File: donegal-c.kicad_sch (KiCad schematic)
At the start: 165 parts, among them J1 Molex-0548190519, J2 ISP, SW1 SW_SPST, SW10 SW_SPST, SW11 SW_SPST, SW12 SW_SPST, SW13 SW_SPST, SW14 SW_SPST, SW15 SW_SPST, SW16 SW_SPST, SW17 SW_SPST, SW18 SW_SPST, SW19 SW_SPST, SW2 SW_SPST, SW20 SW_SPST, SW21 SW_SPST, SW22 SW_SPST, SW23 SW_SPST, SW24 SW_SPST, SW25 SW_SPST, SW26 SW_SPST, SW27 SW_SPST, SW28 SW_SPST, SW29 SW_SPST, SW3 SW_SPST, SW30 SW_SPST, SW31 SW_SPST, SW32 SW_SPST, SW33 SW_SPST, SW34 SW_SPST, SW35 SW_SPST, SW36 SW_SPST, SW37 SW_SPST, SW38 SW_SPST, SW39 SW_SPST, SW4 SW_SPST, SW40 SW_SPST, SW41 SW_SPST, SW42 SW_SPST, SW43 SW_SPST, SW44 SW_SPST, SW45 SW_SPST, SW46 SW_SPST, SW47 SW_SPST, SW48 SW_SPST, SW49 SW_SPST, SW5 SW_SPST, SW50 SW_SPST, SW51 SW_SPST, SW52 SW_SPST, SW53 SW_SPST, SW54 SW_SPST, SW55 SW_SPST, SW56 SW_SPST, SW57 SW_SPST, SW58 SW_SPST, SW59 SW_SPST, SW6 SW_SPST, SW60 SW_SPST, SW61 SW_SPST, SW62 SW_SPST, SW63 SW_SPST, SW64 SW_SPST, SW65 SW_SPST, SW66 SW_SPST, SW67 SW_SPST, SW68 RESET, SW69 BOOT, SW7 SW_SPST, SW70 SW_SPST, SW71 SW_SPST, SW8 SW_SPST, SW9 SW_SPST, U1 ATmega328-PU, Y1 16MHZ

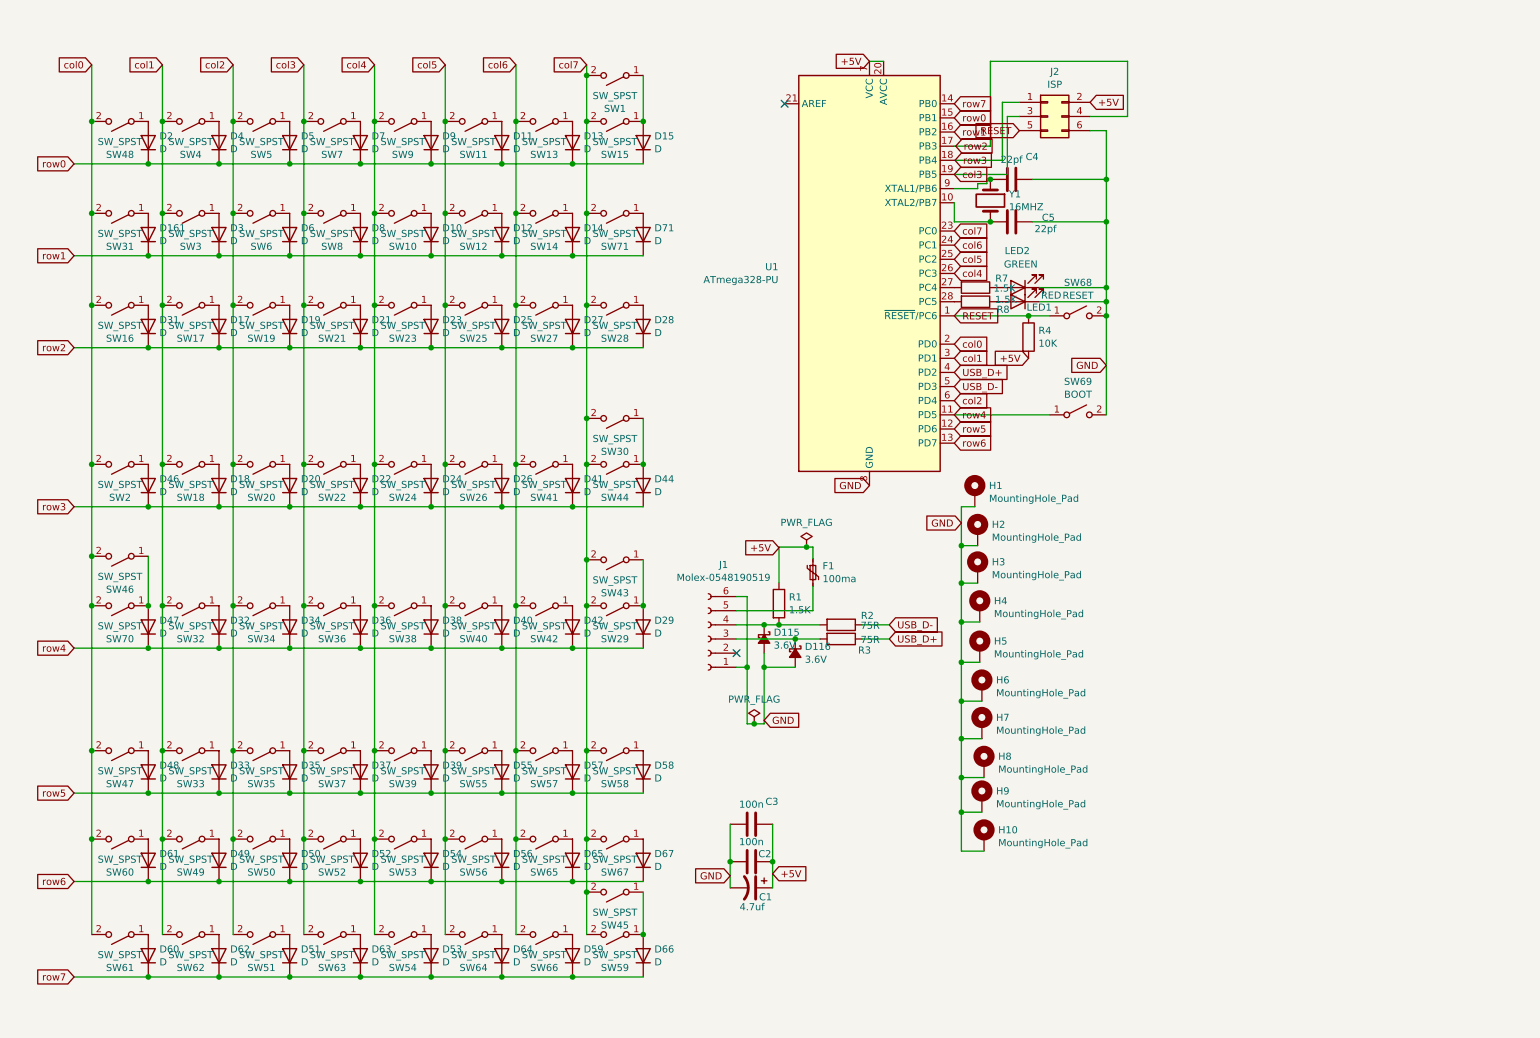
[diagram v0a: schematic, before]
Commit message: Replace Mini USB with USB-C; reroute top and cleanup
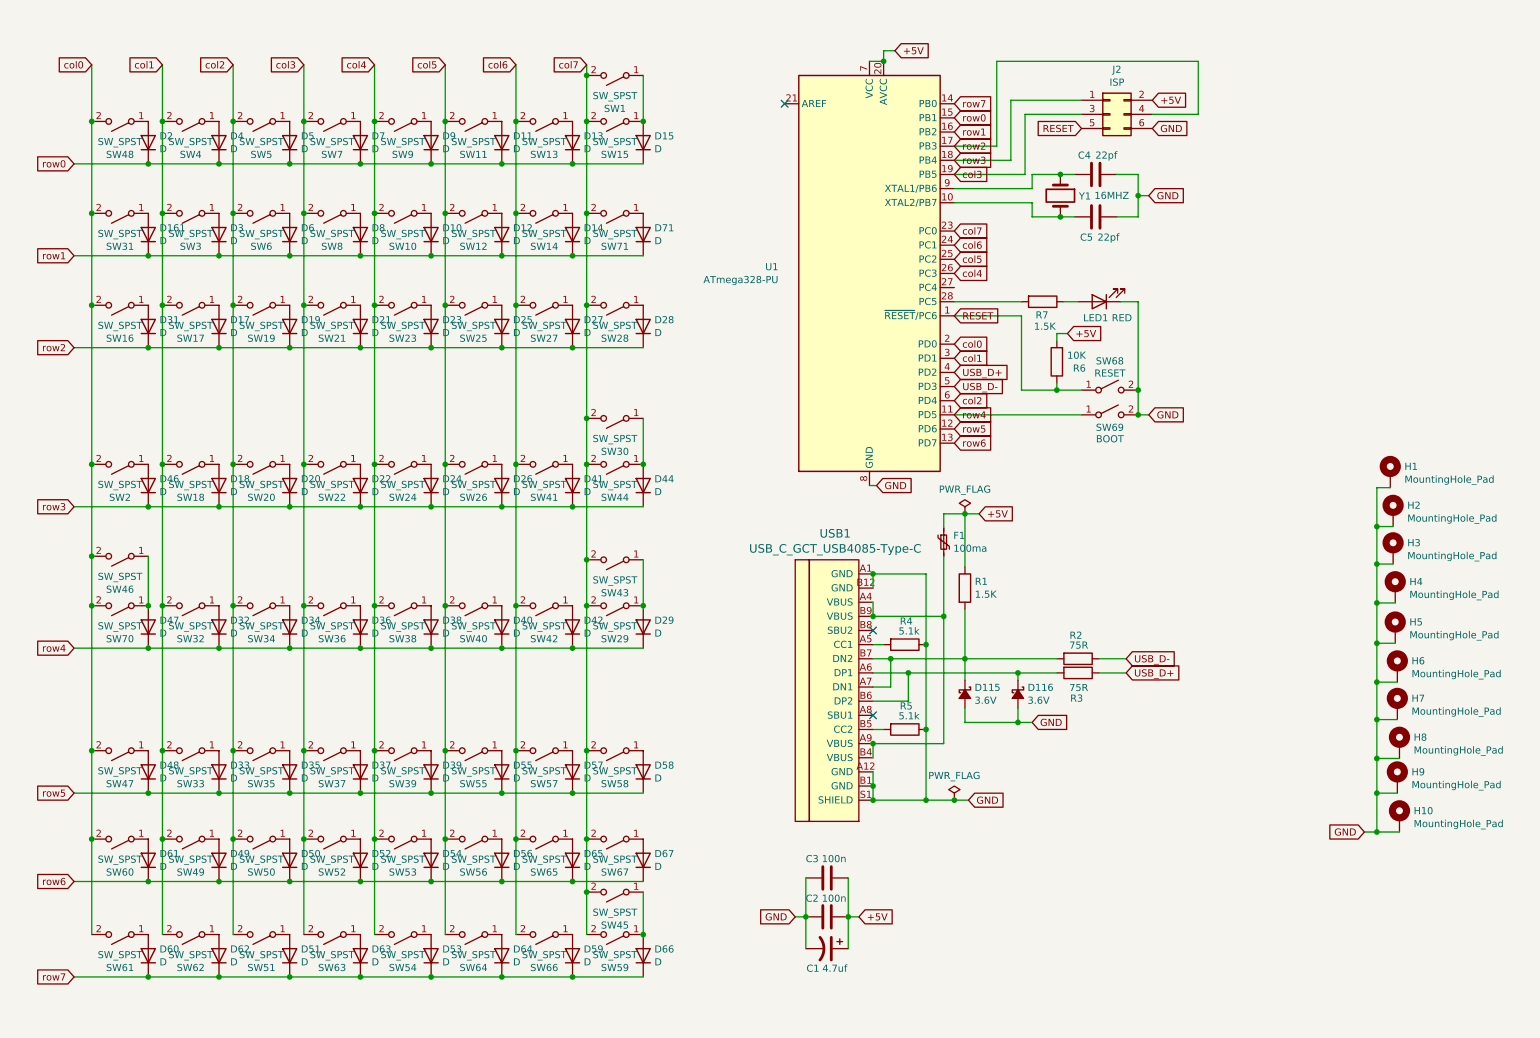
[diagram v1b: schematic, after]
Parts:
- removed J1: Molex-0548190519, random:Molex-0548190519, symbol Connector:Conn_01x06_Female
- removed LED2: GREEN, LED_THT:LED_D3.0mm_Clear, symbol Device:LED
- removed R7: 1.5K, Resistor_THT:R_Axial_DIN0204_L3.6mm_D1.6mm_P5.08mm_Horizontal, symbol Device:R
- added R4, R5: 5.1k, Resistor_THT:R_Axial_DIN0204_L3.6mm_D1.6mm_P5.08mm_Horizontal, symbol Device:R
- added USB1: USB_C_GCT_USB4085-Type-C, tartan:USB_C_GCT_USB4085, symbol donegal-c:USB_C_GCT_USB4085-Type-C
- renumbered R4 to R6, R8 to R7
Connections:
- net GND: now also R4.1, R5.1, USB1.A1 (GND), USB1.A12 (GND), USB1.B1 (GND), USB1.B12 (GND), USB1.S1 (SHIELD)
- net at D116.1 (K), R3.2: now also USB1.A6 (DP1), USB1.B6 (DP2)
- net at D115.1 (K), R1.2, R2.2: now also USB1.A7 (DN1), USB1.B7 (DN2)
- net at F1.2: now also USB1.A4 (VBUS), USB1.A9 (VBUS), USB1.B4 (VBUS), USB1.B9 (VBUS)
- new net: R4.2, USB1.A5 (CC1)
- new net: R5.2, USB1.B5 (CC2)
- no-connect marks 2 -> 3
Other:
- moved on the sheet: C1, C2, C3, C4, C5, D115, D116, F1, H1, H10, H2, H3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

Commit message: Use MX-only switch footprints
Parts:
- added SW72: SW_SPST, tartan:SW_Cherry_MX1A_1.25u_PCBNOSCREEN, symbol Switch:SW_SPST
- SW31: footprint alpsmx:MX-1.75U-NoLED -> tartan:SW_Cherry_MX1A_1.75u_PCBNOSCREEN
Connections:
- net col0: now also SW72.2 (B)
- net at D161.2 (A), SW31.1 (A): now also SW72.1 (A)
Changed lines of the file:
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@@
   (paper "A4")
   (junction (at 24.765 34.29) (diameter 1.016) (color 0 0 0 0))
+  (junction (at 24.765 43.815) (diameter 1.016) (color 0 0 0 0))
   (junction (at 24.765 50.8) (diameter 1.016) (color 0 0 0 0))
   (junction (at 24.765 67.31) (diameter 1.016) (color 0 0 0 0))
@@
   (junction (at 24.765 163.195) (diameter 1.016) (color 0 0 0 0))
   (junction (at 34.925 41.91) (diameter 1.016) (color 0 0 0 0))
+  (junction (at 34.925 50.8) (diameter 1.016) (color 0 0 0 0))
   (junction (at 34.925 58.42) (diameter 1.016) (color 0 0 0 0))
   (junction (at 34.925 74.93) (diameter 1.016) (color 0 0 0 0))
@@
     (stroke (width 0) (type solid) (color 0 0 0 0))
   )
-  (wire (pts (xy 24.765 34.29) (xy 24.765 50.8))
+  (wire (pts (xy 24.765 34.29) (xy 24.765 43.815))
+    (stroke (width 0) (type solid) (color 0 0 0 0))
+  )
+  (wire (pts (xy 24.765 43.815) (xy 24.765 50.8))
     (stroke (width 0) (type solid) (color 0 0 0 0))
   )
@@
     (stroke (width 0) (type solid) (color 0 0 0 0))
   )
+  (wire (pts (xy 34.925 43.815) (xy 34.925 50.8))
+    (stroke (width 0) (type solid) (color 0 0 0 0))
+  )
   (wire (pts (xy 34.925 58.42) (xy 47.625 58.42))
     (stroke (width 0) (type solid) (color 0 0 0 0))
@@
     )
   )
+  (symbol (lib_id "Switch:SW_SPST") (at 29.845 43.815 180) (unit 1)
+    (in_bom yes) (on_board yes)
+    (property "Reference" "SW72" (id 0) (at 29.845 49.784 0))
+    (property "Value" "SW_SPST" (id 1) (at 29.845 47.4726 0))
+    (property "Footprint" "tartan:SW_Cherry_MX1A_1.25u_PCBNOSCREEN" (id 2) (at 29.845 43.815 0)
+      (effects (font (size 1.27 1.27)) hide)
+    )
+    (property "Datasheet" "~" (id 3) (at 29.845 43.815 0)
+      (effects (font (size 1.27 1.27)) hide)
+    )
+  )
   (symbol (lib_id "Switch:SW_SPST") (at 29.845 50.8 180) (unit 1)
     (in_bom yes) (on_board yes)
     (property "Reference" "SW31" (id 0) (at 29.845 56.769 0))
     (property "Value" "SW_SPST" (id 1) (at 29.845 54.4576 0))
-    (property "Footprint" "alpsmx:MX-1.75U-NoLED" (id 2) (at 29.845 50.8 0)
+    (property "Footprint" "tartan:SW_Cherry_MX1A_1.75u_PCBNOSCREEN" (id 2) (at 29.845 50.8 0)
       (effects (font (size 1.27 1.27)) hide)
     )
@@
     )
     (path "/00000000-0000-0000-0000-00005dff720a"
-      (reference "SW31") (unit 1) (value "SW_SPST") (footprint "alpsmx:MX-1.75U-NoLED")
+      (reference "SW31") (unit 1) (value "SW_SPST") (footprint "tartan:SW_Cherry_MX1A_1.75u_PCBNOSCREEN")
     )
     (path "/00000000-0000-0000-0000-00005e04c632"
@@
       (reference "SW71") (unit 1) (value "SW_SPST") (footprint "alpsmx:MX-1U-NoLED")
     )
+    (path "/3b7836b9-0d41-4603-addd-d5e0443b07f1"
+      (reference "SW72") (unit 1) (value "SW_SPST") (footprint "tartan:SW_Cherry_MX1A_1.25u_PCBNOSCREEN")
+    )
     (path "/00000000-0000-0000-0000-00005e1cc4c5"

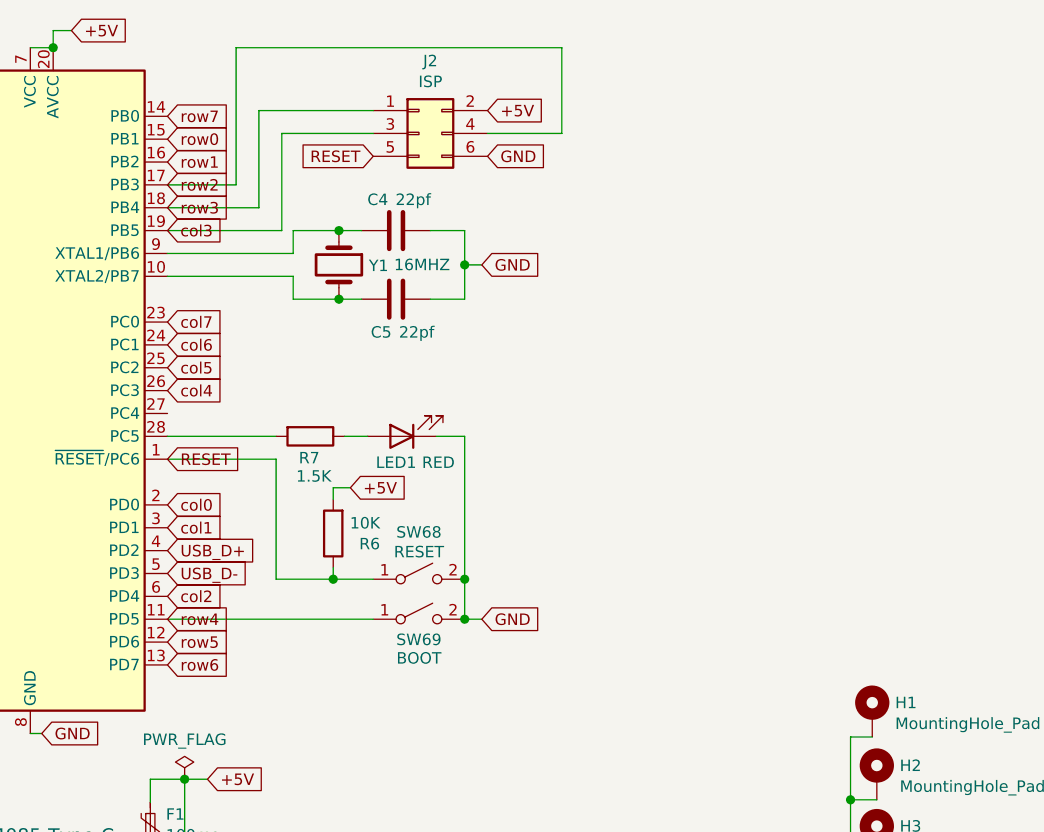
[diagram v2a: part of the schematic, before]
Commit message: Add component values to the silk screen
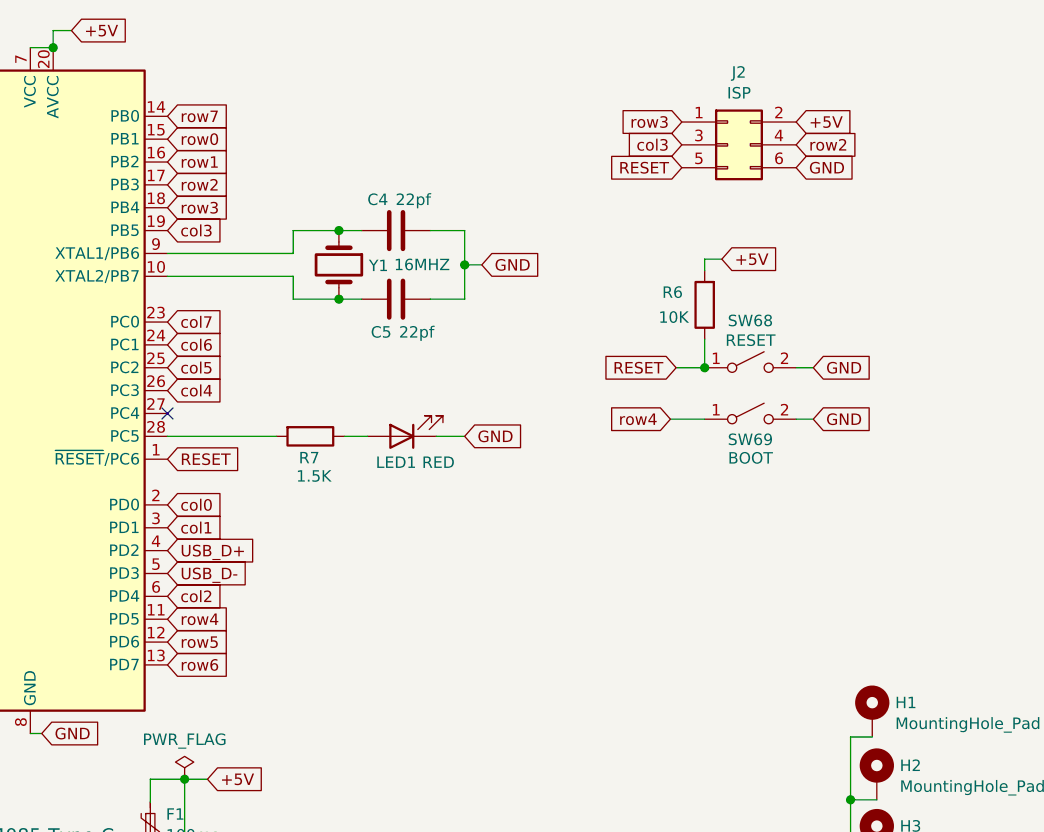
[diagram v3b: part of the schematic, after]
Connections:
- no-connect marks 3 -> 4
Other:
- moved on the sheet: J2, R6, SW68, SW69
